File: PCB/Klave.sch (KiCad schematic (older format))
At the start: 19 parts

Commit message: Add key matrix
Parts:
- added D? (x31): D_Small, symbol Device:D_Small
- added SW? (x31): SW_Key, symbol Switch:SW_Push
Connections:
- net col2: now reaches U?.10 (7|E6)
- net col2: now also SW?.1, SW?.1, SW?.1, SW?.1, SW?.1
- net col1: now reaches U?.11 (8|B4)
- net col1: now also SW?.1, SW?.1, SW?.1, SW?.1, SW?.1
- net col0: now reaches U?.12 (9|B5)
- net col0: now also SW?.1, SW?.1, SW?.1, SW?.1
- net row0: now reaches U?.13 (B6|10)
- net row0: now also D?.1 (K), D?.1 (K), D?.1 (K), D?.1 (K), D?.1 (K), D?.1 (K)
- net row1: now reaches U?.14 (B2|16)
- net row1: now also D?.1 (K), D?.1 (K), D?.1 (K), D?.1 (K), D?.1 (K), D?.1 (K)
- net row2: now reaches U?.15 (B3|14)
- net row2: now also D?.1 (K), D?.1 (K), D?.1 (K), D?.1 (K), D?.1 (K), D?.1 (K)
- net row3: now reaches U?.16 (B1|15)
- net row3: now also D?.1 (K), D?.1 (K), D?.1 (K), D?.1 (K), D?.1 (K), D?.1 (K)
- net row4: now reaches U?.17 (F7|A0)
- net row4: now also D?.1 (K), D?.1 (K), D?.1 (K), D?.1 (K), D?.1 (K)
- net row5: now reaches U?.18 (F6|A1)
- net row5: now also D?.1 (K), D?.1 (K)
- net col5: now reaches U?.7 (4|D4)
- net col5: now also SW?.1, SW?.1, SW?.1, SW?.1, SW?.1, SW?.1
- net col4: now reaches U?.8 (5|C6)
- net col4: now also SW?.1, SW?.1, SW?.1, SW?.1, SW?.1, SW?.1
- net col3: now reaches U?.9 (6|D7)
- net col3: now also SW?.1, SW?.1, SW?.1, SW?.1, SW?.1
- new net: D?.2 (A), SW?.2 (x31)
- no-connect marks 16 -> 4

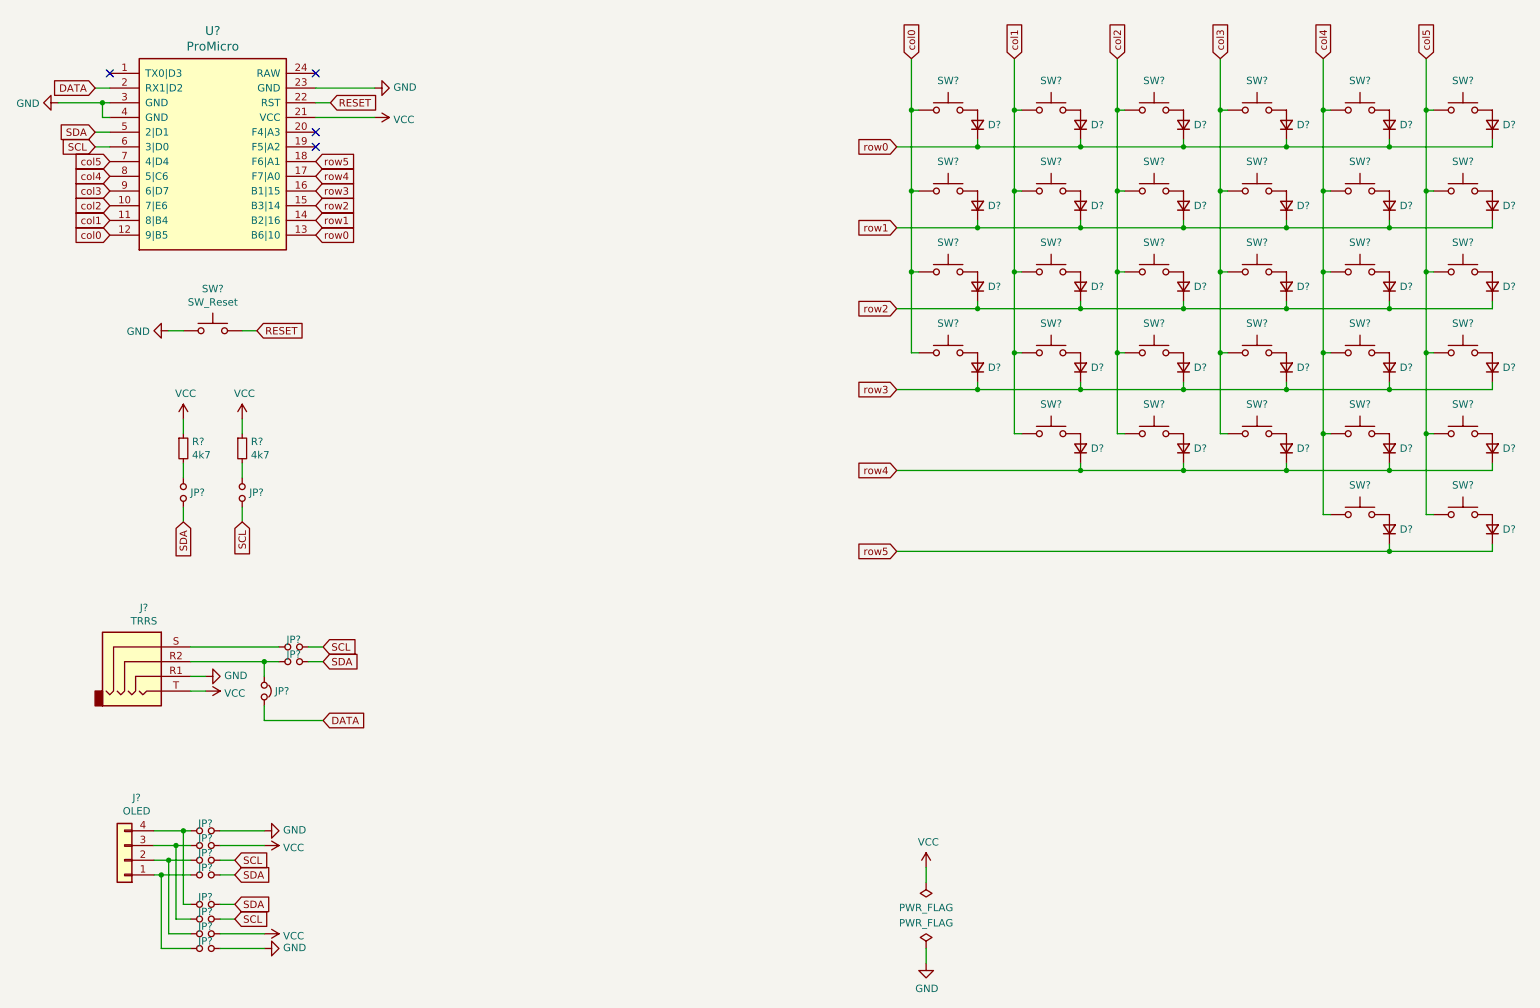
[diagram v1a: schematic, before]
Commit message: Add rotary encoder switch
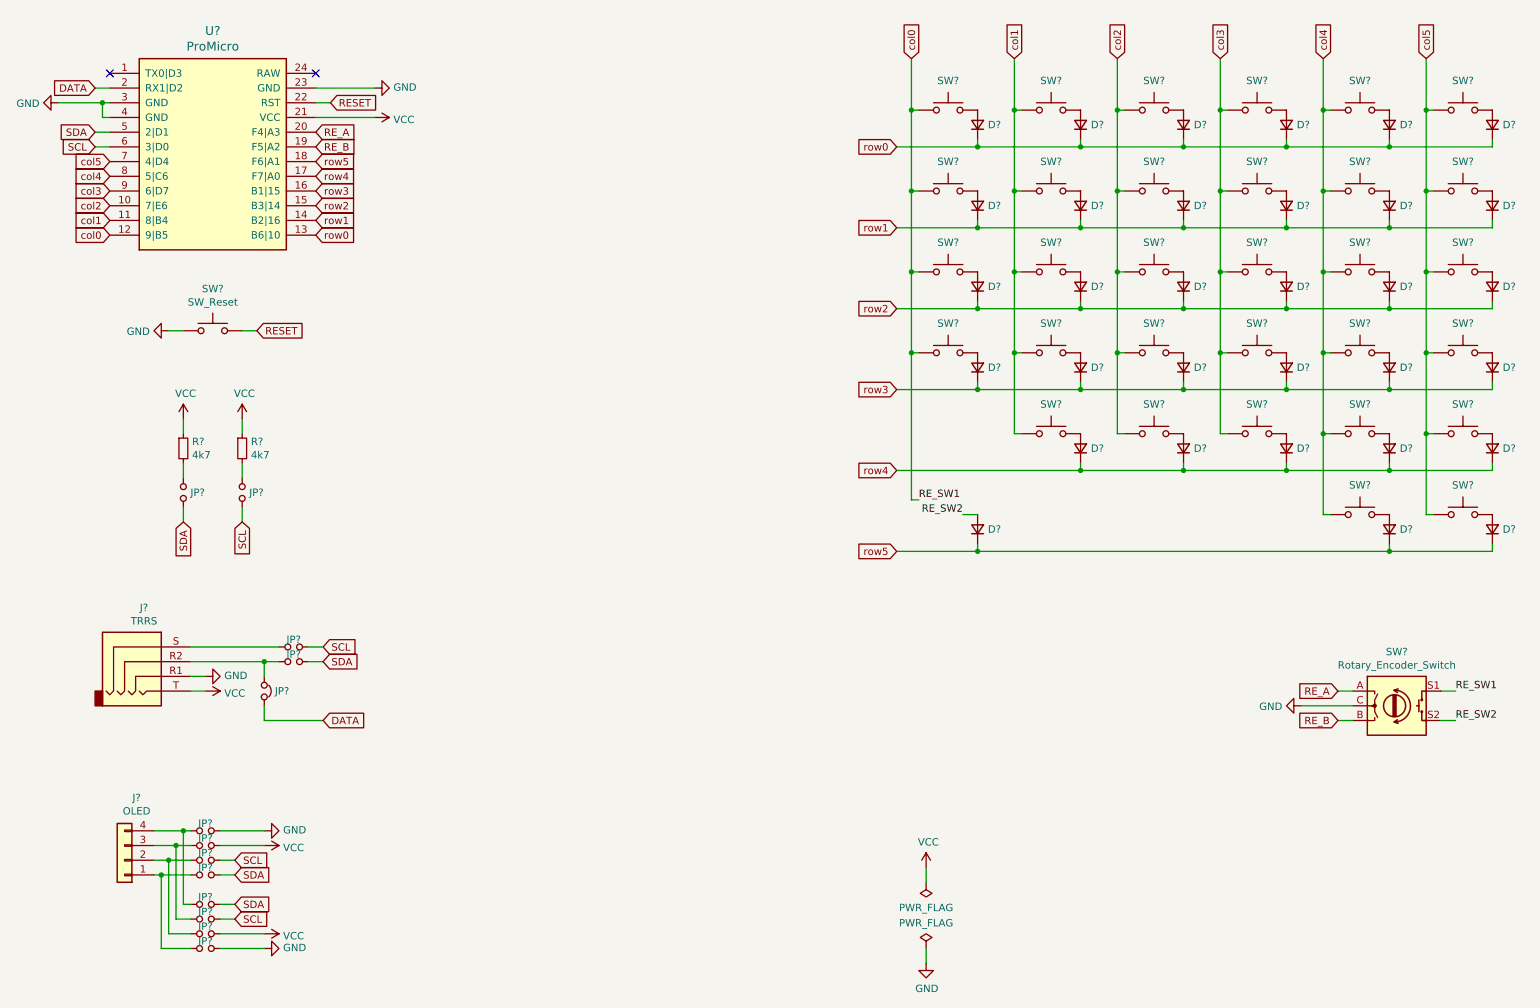
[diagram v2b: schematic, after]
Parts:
- added D?: D_Small, symbol Device:D_Small
- added SW?: Rotary_Encoder_Switch, symbol Device:Rotary_Encoder_Switch
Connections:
- net GND: now also SW?.C
- net col0: now also SW?.S1
- net row5: now also D?.1 (K)
- net RE_B: now reaches U?.19 (F5|A2)
- net RE_B: now also SW?.B
- net RE_A: now reaches U?.20 (F4|A3)
- net RE_A: now also SW?.A
- new net RE_SW2: D?.2 (A), SW?.S2
- no-connect marks 4 -> 2
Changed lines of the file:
@@
 RESET
 NoConn ~ 2550 1450
-NoConn ~ 2550 1950
-NoConn ~ 2550 1850
 $Comp
 L power:GND #PWR?
@@
 Connection ~ 10100 3900
 Wire Wire Line
-	6500 4700 9850 4700
+	6500 4700 7050 4700
+$Comp
+L Device:Rotary_Encoder_Switch SW?
+U 1 1 5F65CF2A
+P 9900 5750
+F 0 "SW?" H 9900 6117 50  0000 C CNN
+F 1 "Rotary_Encoder_Switch" H 9900 6026 50  0000 C CNN
+F 2 "" H 9750 5910 50  0001 C CNN
+F 3 "~" H 9900 6010 50  0001 C CNN
+	1    9900 5750
+	1    0    0    -1
+$EndComp
+$Comp
+L Device:D_Small D?
+U 1 1 5F66CA7F
+P 7050 4550
+F 0 "D?" V 7050 4480 50  0000 R CNN
+F 1 "D_Small" V 7005 4480 50  0001 R CNN
+F 2 "" V 7050 4550 50  0001 C CNN
+F 3 "~" V 7050 4550 50  0001 C CNN
+	1    7050 4550
+	0    -1   -1   0
+$EndComp
+Wire Wire Line
+	7050 4650 7050 4700
+Connection ~ 7050 4700
+Wire Wire Line
+	7050 4700 9850 4700
+Wire Wire Line
+	6650 4350 6600 4350
+Wire Wire Line
+	6600 4350 6600 3350
+Connection ~ 6600 3350
+$Comp
+L power:GND #PWR?
+U 1 1 5F686B26
+P 9250 5750
+F 0 "#PWR?" H 9250 5500 50  0001 C CNN
+F 1 "GND" V 9255 5622 50  0000 R CNN
+F 2 "" H 9250 5750 50  0001 C CNN
+F 3 "" H 9250 5750 50  0001 C CNN
+	1    9250 5750
+	0    1    1    0
+$EndComp
+Wire Wire Line
+	9600 5750 9250 5750
+Text GLabel 2550 1850 2    50   Input ~ 0
+RE_A
+Text GLabel 2550 1950 2    50   Input ~ 0
+RE_B
+Text GLabel 9500 5850 0    50   Input ~ 0
+RE_B
+Text GLabel 9500 5650 0    50   Input ~ 0
+RE_A
+Wire Wire Line
+	9600 5650 9500 5650
+Wire Wire Line
+	9600 5850 9500 5850
+Wire Wire Line
+	10200 5650 10300 5650
+Wire Wire Line
+	10200 5850 10300 5850
+Text Label 10300 5650 0    50   ~ 0
+RE_SW1
+Text Label 10300 5850 0    50   ~ 0
+RE_SW2
+Text Label 6650 4350 0    50   ~ 0
+RE_SW1
+Text Label 6950 4450 2    50   ~ 0
+RE_SW2
+Wire Wire Line
+	7050 4450 6950 4450
 $EndSCHEMATC

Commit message: Edit schematic
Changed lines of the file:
@@
 Text GLabel 6500 3600 0    50   Input ~ 0
 row3
-Text GLabel 1150 2550 0    50   Input ~ 0
+Text GLabel 1050 2550 0    50   Input ~ 0
 col0
-Text GLabel 1150 2450 0    50   Input ~ 0
+Text GLabel 1050 2450 0    50   Input ~ 0
 col1
-Text GLabel 1150 2350 0    50   Input ~ 0
+Text GLabel 1050 2350 0    50   Input ~ 0
 col2
-Text GLabel 1150 2250 0    50   Input ~ 0
+Text GLabel 1050 2250 0    50   Input ~ 0
 col3
-Text GLabel 2550 2550 2    50   Input ~ 0
+Text GLabel 2650 2550 2    50   Input ~ 0
 row0
-Text GLabel 2550 2450 2    50   Input ~ 0
+Text GLabel 2650 2450 2    50   Input ~ 0
 row1
-Text GLabel 2550 2350 2    50   Input ~ 0
+Text GLabel 2650 2350 2    50   Input ~ 0
 row2
-Text GLabel 2550 2250 2    50   Input ~ 0
+Text GLabel 2650 2250 2    50   Input ~ 0
 row3
-Text GLabel 2550 2150 2    50   Input ~ 0
+Text GLabel 2650 2150 2    50   Input ~ 0
 row4
-Text GLabel 1150 2150 0    50   Input ~ 0
+Text GLabel 1050 2150 0    50   Input ~ 0
 col4
-Text GLabel 1150 2050 0    50   Input ~ 0
+Text GLabel 1050 2050 0    50   Input ~ 0
 col5
 $Comp
@@
 Text GLabel 6500 4700 0    50   Input ~ 0
 row5
-Text GLabel 2550 2050 2    50   Input ~ 0
+Text GLabel 2650 2050 2    50   Input ~ 0
 row5
 $Comp
@@
 Wire Wire Line
 	9600 5750 9250 5750
-Text GLabel 2550 1850 2    50   Input ~ 0
+Text GLabel 2650 1850 2    50   Input ~ 0
 RE_A
-Text GLabel 2550 1950 2    50   Input ~ 0
+Text GLabel 2650 1950 2    50   Input ~ 0
 RE_B
 Text GLabel 9500 5850 0    50   Input ~ 0
@@
 Wire Wire Line
 	7050 4450 6950 4450
+Wire Wire Line
+	1050 2050 1150 2050
+Wire Wire Line
+	1150 2150 1050 2150
+Wire Wire Line
+	1050 2250 1150 2250
+Wire Wire Line
+	1050 2350 1150 2350
+Wire Wire Line
+	1150 2450 1050 2450
+Wire Wire Line
+	1050 2550 1150 2550
+Wire Wire Line
+	2550 2550 2650 2550
+Wire Wire Line
+	2650 2450 2550 2450
+Wire Wire Line
+	2550 2350 2650 2350
+Wire Wire Line
+	2650 2250 2550 2250
+Wire Wire Line
+	2550 2150 2650 2150
+Wire Wire Line
+	2650 2050 2550 2050
+Wire Wire Line
+	2550 1950 2650 1950
+Wire Wire Line
+	2650 1850 2550 1850
 $EndSCHEMATC

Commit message: Annotate schematic symbols
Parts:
- gave numbers to parts that had none: 82
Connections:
- net RE_A renamed E31_A
- net RE_B renamed E31_B
- net RE_SW2 renamed SW31_2

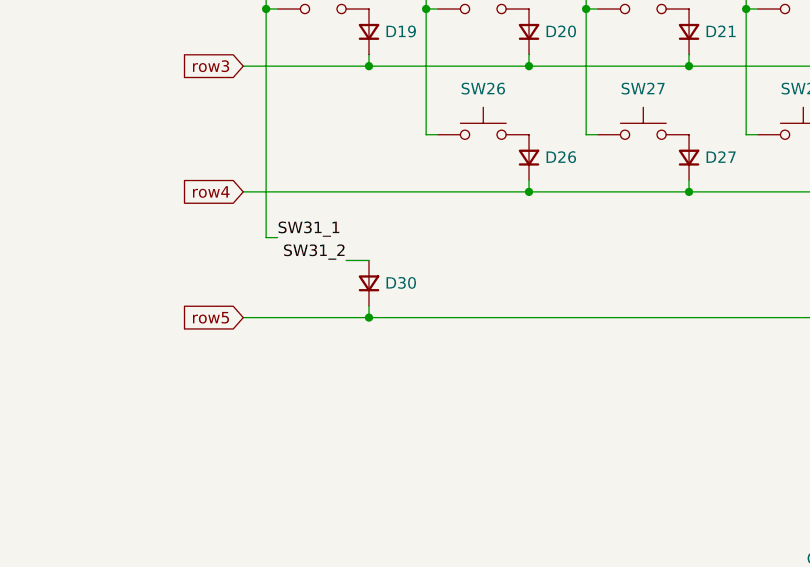
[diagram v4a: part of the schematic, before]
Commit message: Fix schematic symbol reference
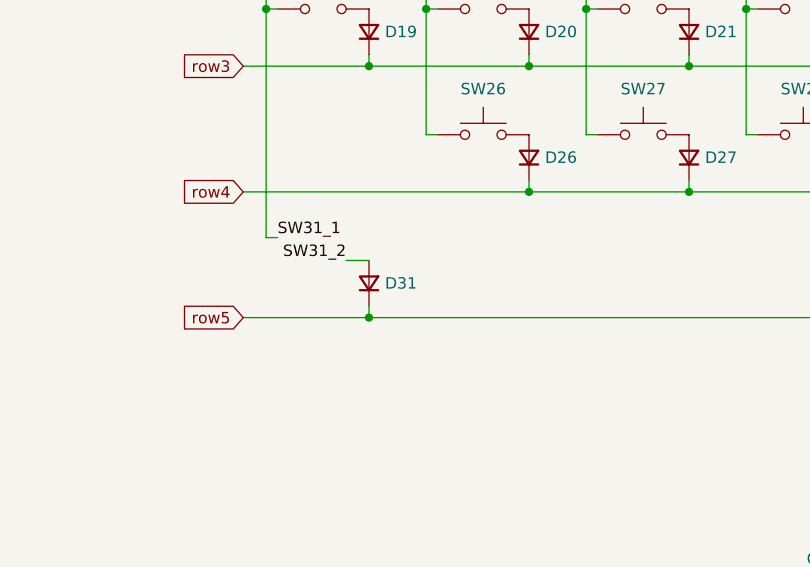
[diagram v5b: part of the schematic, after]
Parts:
- renumbered D30 to D31
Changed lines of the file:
@@
 $EndComp
 $Comp
-L Device:D_Small D30
+L Device:D_Small D31
 U 1 1 5F66CA7F
 P 7050 4550
-F 0 "D30" V 7050 4480 50  0000 R CNN
+F 0 "D31" V 7050 4480 50  0000 R CNN
 F 1 "D_Small" V 7005 4480 50  0001 R CNN
 F 2 "" V 7050 4550 50  0001 C CNN

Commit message: Rename key diodes
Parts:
- D1, D10, D11, D12, D13, D14, D15, D16, D17, D18, D19, D2, D20, D21, D22, D23, D24, D26, D27, D28, D29, D3, D30, D31, D35, D36, D4, D5, D6, D7, D8, D9: value D_Small -> D_Key
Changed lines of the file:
@@
 P 7050 1800
 F 0 "D1" V 7050 1730 50  0000 R CNN
-F 1 "D_Small" V 7005 1730 50  0001 R CNN
+F 1 "D_Key" V 7005 1730 50  0001 R CNN
 F 2 "" V 7050 1800 50  0001 C CNN
 F 3 "~" V 7050 1800 50  0001 C CNN
@@
 P 7750 1800
 F 0 "D2" V 7750 1730 50  0000 R CNN
-F 1 "D_Small" V 7705 1730 50  0001 R CNN
+F 1 "D_Key" V 7705 1730 50  0001 R CNN
 F 2 "" V 7750 1800 50  0001 C CNN
 F 3 "~" V 7750 1800 50  0001 C CNN
@@
 P 8450 1800
 F 0 "D3" V 8450 1730 50  0000 R CNN
-F 1 "D_Small" V 8405 1730 50  0001 R CNN
+F 1 "D_Key" V 8405 1730 50  0001 R CNN
 F 2 "" V 8450 1800 50  0001 C CNN
 F 3 "~" V 8450 1800 50  0001 C CNN
@@
 P 9150 1800
 F 0 "D4" V 9150 1730 50  0000 R CNN
-F 1 "D_Small" V 9105 1730 50  0001 R CNN
+F 1 "D_Key" V 9105 1730 50  0001 R CNN
 F 2 "" V 9150 1800 50  0001 C CNN
 F 3 "~" V 9150 1800 50  0001 C CNN
@@
 P 9850 1800
 F 0 "D5" V 9850 1730 50  0000 R CNN
-F 1 "D_Small" V 9805 1730 50  0001 R CNN
+F 1 "D_Key" V 9805 1730 50  0001 R CNN
 F 2 "" V 9850 1800 50  0001 C CNN
 F 3 "~" V 9850 1800 50  0001 C CNN
@@
 P 10550 1800
 F 0 "D6" V 10550 1730 50  0000 R CNN
-F 1 "D_Small" V 10505 1730 50  0001 R CNN
+F 1 "D_Key" V 10505 1730 50  0001 R CNN
 F 2 "" V 10550 1800 50  0001 C CNN
 F 3 "~" V 10550 1800 50  0001 C CNN
@@
 P 10550 3450
 F 0 "D24" V 10550 3380 50  0000 R CNN
-F 1 "D_Small" V 10505 3380 50  0001 R CNN
+F 1 "D_Key" V 10505 3380 50  0001 R CNN
 F 2 "" V 10550 3450 50  0001 C CNN
 F 3 "~" V 10550 3450 50  0001 C CNN
@@
 P 10550 2900
 F 0 "D18" V 10550 2830 50  0000 R CNN
-F 1 "D_Small" V 10505 2830 50  0001 R CNN
+F 1 "D_Key" V 10505 2830 50  0001 R CNN
 F 2 "" V 10550 2900 50  0001 C CNN
 F 3 "~" V 10550 2900 50  0001 C CNN
@@
 P 10550 2350
 F 0 "D12" V 10550 2280 50  0000 R CNN
-F 1 "D_Small" V 10505 2280 50  0001 R CNN
+F 1 "D_Key" V 10505 2280 50  0001 R CNN
 F 2 "" V 10550 2350 50  0001 C CNN
 F 3 "~" V 10550 2350 50  0001 C CNN
@@
 P 9850 3450
 F 0 "D23" V 9850 3380 50  0000 R CNN
-F 1 "D_Small" V 9805 3380 50  0001 R CNN
+F 1 "D_Key" V 9805 3380 50  0001 R CNN
 F 2 "" V 9850 3450 50  0001 C CNN
 F 3 "~" V 9850 3450 50  0001 C CNN
@@
 P 9850 2900
 F 0 "D17" V 9850 2830 50  0000 R CNN
-F 1 "D_Small" V 9805 2830 50  0001 R CNN
+F 1 "D_Key" V 9805 2830 50  0001 R CNN
 F 2 "" V 9850 2900 50  0001 C CNN
 F 3 "~" V 9850 2900 50  0001 C CNN
@@
 P 9850 2350
 F 0 "D11" V 9850 2280 50  0000 R CNN
-F 1 "D_Small" V 9805 2280 50  0001 R CNN
+F 1 "D_Key" V 9805 2280 50  0001 R CNN
 F 2 "" V 9850 2350 50  0001 C CNN
 F 3 "~" V 9850 2350 50  0001 C CNN
@@
 P 9150 3450
 F 0 "D22" V 9150 3380 50  0000 R CNN
-F 1 "D_Small" V 9105 3380 50  0001 R CNN
+F 1 "D_Key" V 9105 3380 50  0001 R CNN
 F 2 "" V 9150 3450 50  0001 C CNN
 F 3 "~" V 9150 3450 50  0001 C CNN
@@
 P 9150 2900
 F 0 "D16" V 9150 2830 50  0000 R CNN
-F 1 "D_Small" V 9105 2830 50  0001 R CNN
+F 1 "D_Key" V 9105 2830 50  0001 R CNN
 F 2 "" V 9150 2900 50  0001 C CNN
 F 3 "~" V 9150 2900 50  0001 C CNN
@@
 P 9150 2350
 F 0 "D10" V 9150 2280 50  0000 R CNN
-F 1 "D_Small" V 9105 2280 50  0001 R CNN
+F 1 "D_Key" V 9105 2280 50  0001 R CNN
 F 2 "" V 9150 2350 50  0001 C CNN
 F 3 "~" V 9150 2350 50  0001 C CNN
@@
 P 8450 3450
 F 0 "D21" V 8450 3380 50  0000 R CNN
-F 1 "D_Small" V 8405 3380 50  0001 R CNN
+F 1 "D_Key" V 8405 3380 50  0001 R CNN
 F 2 "" V 8450 3450 50  0001 C CNN
 F 3 "~" V 8450 3450 50  0001 C CNN
@@
 P 8450 2900
 F 0 "D15" V 8450 2830 50  0000 R CNN
-F 1 "D_Small" V 8405 2830 50  0001 R CNN
+F 1 "D_Key" V 8405 2830 50  0001 R CNN
 F 2 "" V 8450 2900 50  0001 C CNN
 F 3 "~" V 8450 2900 50  0001 C CNN
@@
 P 8450 2350
 F 0 "D9" V 8450 2280 50  0000 R CNN
-F 1 "D_Small" V 8405 2280 50  0001 R CNN
+F 1 "D_Key" V 8405 2280 50  0001 R CNN
 F 2 "" V 8450 2350 50  0001 C CNN
 F 3 "~" V 8450 2350 50  0001 C CNN
@@
 P 7750 3450
 F 0 "D20" V 7750 3380 50  0000 R CNN
-F 1 "D_Small" V 7705 3380 50  0001 R CNN
+F 1 "D_Key" V 7705 3380 50  0001 R CNN
 F 2 "" V 7750 3450 50  0001 C CNN
 F 3 "~" V 7750 3450 50  0001 C CNN
@@
 P 7750 2900
 F 0 "D14" V 7750 2830 50  0000 R CNN
-F 1 "D_Small" V 7705 2830 50  0001 R CNN
+F 1 "D_Key" V 7705 2830 50  0001 R CNN
 F 2 "" V 7750 2900 50  0001 C CNN
 F 3 "~" V 7750 2900 50  0001 C CNN
@@
 P 7750 2350
 F 0 "D8" V 7750 2280 50  0000 R CNN
-F 1 "D_Small" V 7705 2280 50  0001 R CNN
+F 1 "D_Key" V 7705 2280 50  0001 R CNN
 F 2 "" V 7750 2350 50  0001 C CNN
 F 3 "~" V 7750 2350 50  0001 C CNN
@@
 P 7050 3450
 F 0 "D19" V 7050 3380 50  0000 R CNN
-F 1 "D_Small" V 7005 3380 50  0001 R CNN
+F 1 "D_Key" V 7005 3380 50  0001 R CNN
 F 2 "" V 7050 3450 50  0001 C CNN
 F 3 "~" V 7050 3450 50  0001 C CNN
@@
 P 7050 2900
 F 0 "D13" V 7050 2830 50  0000 R CNN
-F 1 "D_Small" V 7005 2830 50  0001 R CNN
+F 1 "D_Key" V 7005 2830 50  0001 R CNN
 F 2 "" V 7050 2900 50  0001 C CNN
 F 3 "~" V 7050 2900 50  0001 C CNN
@@
 P 7050 2350
 F 0 "D7" V 7050 2280 50  0000 R CNN
-F 1 "D_Small" V 7005 2280 50  0001 R CNN
+F 1 "D_Key" V 7005 2280 50  0001 R CNN
 F 2 "" V 7050 2350 50  0001 C CNN
 F 3 "~" V 7050 2350 50  0001 C CNN
@@
 P 10550 4000
 F 0 "D30" V 10550 3930 50  0000 R CNN
-F 1 "D_Small" V 10505 3930 50  0001 R CNN
+F 1 "D_Key" V 10505 3930 50  0001 R CNN
 F 2 "" V 10550 4000 50  0001 C CNN
 F 3 "~" V 10550 4000 50  0001 C CNN
@@
 P 9850 4000
 F 0 "D29" V 9850 3930 50  0000 R CNN
-F 1 "D_Small" V 9805 3930 50  0001 R CNN
+F 1 "D_Key" V 9805 3930 50  0001 R CNN
 F 2 "" V 9850 4000 50  0001 C CNN
 F 3 "~" V 9850 4000 50  0001 C CNN
@@
 P 9150 4000
 F 0 "D28" V 9150 3930 50  0000 R CNN
-F 1 "D_Small" V 9105 3930 50  0001 R CNN
+F 1 "D_Key" V 9105 3930 50  0001 R CNN
 F 2 "" V 9150 4000 50  0001 C CNN
 F 3 "~" V 9150 4000 50  0001 C CNN
@@
 P 8450 4000
 F 0 "D27" V 8450 3930 50  0000 R CNN
-F 1 "D_Small" V 8405 3930 50  0001 R CNN
+F 1 "D_Key" V 8405 3930 50  0001 R CNN
 F 2 "" V 8450 4000 50  0001 C CNN
 F 3 "~" V 8450 4000 50  0001 C CNN
@@
 P 7750 4000
 F 0 "D26" V 7750 3930 50  0000 R CNN
-F 1 "D_Small" V 7705 3930 50  0001 R CNN
+F 1 "D_Key" V 7705 3930 50  0001 R CNN
 F 2 "" V 7750 4000 50  0001 C CNN
 F 3 "~" V 7750 4000 50  0001 C CNN
@@
 P 10550 4550
 F 0 "D36" V 10550 4480 50  0000 R CNN
-F 1 "D_Small" V 10505 4480 50  0001 R CNN
+F 1 "D_Key" V 10505 4480 50  0001 R CNN
 F 2 "" V 10550 4550 50  0001 C CNN
 F 3 "~" V 10550 4550 50  0001 C CNN
@@
 P 9850 4550
 F 0 "D35" V 9850 4480 50  0000 R CNN
-F 1 "D_Small" V 9805 4480 50  0001 R CNN
+F 1 "D_Key" V 9805 4480 50  0001 R CNN
 F 2 "" V 9850 4550 50  0001 C CNN
 F 3 "~" V 9850 4550 50  0001 C CNN
@@
 P 7050 4550
 F 0 "D31" V 7050 4480 50  0000 R CNN
-F 1 "D_Small" V 7005 4480 50  0001 R CNN
+F 1 "D_Key" V 7005 4480 50  0001 R CNN
 F 2 "" V 7050 4550 50  0001 C CNN
 F 3 "~" V 7050 4550 50  0001 C CNN
